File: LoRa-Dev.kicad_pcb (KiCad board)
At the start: 4 copper layers, 72.5 x 71 mm, 19 parts, among them J2 Barrel_Jack_MountingPin, J3 Conn_Coaxial_Small, U1 RPi Pico, U2 LT1963AEQ, U3 RFM95PW

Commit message: E22-900M30S
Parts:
- removed C3: 0.1uF, Capacitor_SMD:C_0603_1608Metric
- removed C4: 47uF, Capacitor_SMD:CP_Elec_6.3x5.8
- removed J3: Conn_Coaxial_Small, Connector_Coaxial:U.FL_Hirose_U.FL-R-SMT-1_Vertical
- removed U3: RFM95PW, LoRa-Dev:RFM95PW
- added C5: 0.1uF, Capacitor_SMD:C_0603_1608Metric, F.Cu at (124.7, 65.5)
- added C6: 47uF, Capacitor_SMD:CP_Elec_6.3x5.8, F.Cu at (125.8, 59.0)
- added J1: Conn_Coaxial_Small, Connector_Coaxial:U.FL_Hirose_U.FL-R-SMT-1_Vertical, F.Cu at (105.2, 53.5)
- added U4: E22-900M30S-SX1262, LoRa-Dev:E22-900M30S-SX1262, F.Cu at (106.8, 79.2)
- moved R9 1.50 mm to (93.5, 48.1)
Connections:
- U1 pad 26: /DIO0 -> /DIO2
- U1 pad 31: unconnected-(U1-GP26-Pad31) -> /BUSY
- U1 pad 32: unconnected-(U1-GP27-Pad32) -> /RXEN
- U1 pad 34: unconnected-(U1-GP28-Pad34) -> /TXEN
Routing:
- net /TXEN: track 0.00 -> 97.2 mm, vias 0 -> 1
- net /RXEN: track 0.00 -> 87.5 mm, vias 0 -> 1
- net /DIO2: track 0.00 -> 55.9 mm, vias 0 -> 2
- net /DIO0: track 52.3 -> 0.00 mm, vias 4 -> 0
- net /BUSY: track 0.00 -> 48.9 mm, vias 0 -> 1
- net GND: track 20.8 -> 52.1 mm, vias 50 -> 54
- net /RESETn: track 25.4 -> 42.8 mm, vias 0 -> 2
- net /SPI_CSn: track 47.3 -> 31.3 mm, vias 3 -> 1
- net /ANT: track 11.1 -> 19.7 mm
- net /DIO1: track 54.5 -> 50.8 mm, vias 4 -> 1
- net /SPI_MISO: track 43.1 -> 39.9 mm
- net /SPI_SCK: track 36.2 -> 33.0 mm
- net RF_VDD: track 109.1 -> 111.7 mm
- net /SPI_MOSI: track 36.4 -> 35.4 mm
- net /RF_GND: vias 29 -> 28

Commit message: updated after first review
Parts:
- removed C6: 47uF, Capacitor_SMD:CP_Elec_6.3x5.8
- added C3: 47uf, Capacitor_SMD:C_1210_3225Metric, F.Cu at (126.8, 59.2)
- moved C5 2.02 mm to (126.7, 65.8)
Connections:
- U4 pad 1: GND -> /RF_GND
- U4 pad 2: GND -> /RF_GND
- U4 pad 20: GND -> /RF_GND
- U4 pad 22: GND -> /RF_GND
- U4 pad 3: GND -> /RF_GND
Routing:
- net GND: track 52.1 -> 20.8 mm, vias 54 -> 46
- net RF_VDD: track 111.7 -> 117.2 mm, vias 6 -> 5
- net /RF_GND: track 0.00 -> 0.90 mm
- net /TXEN: track 97.2 -> 96.4 mm

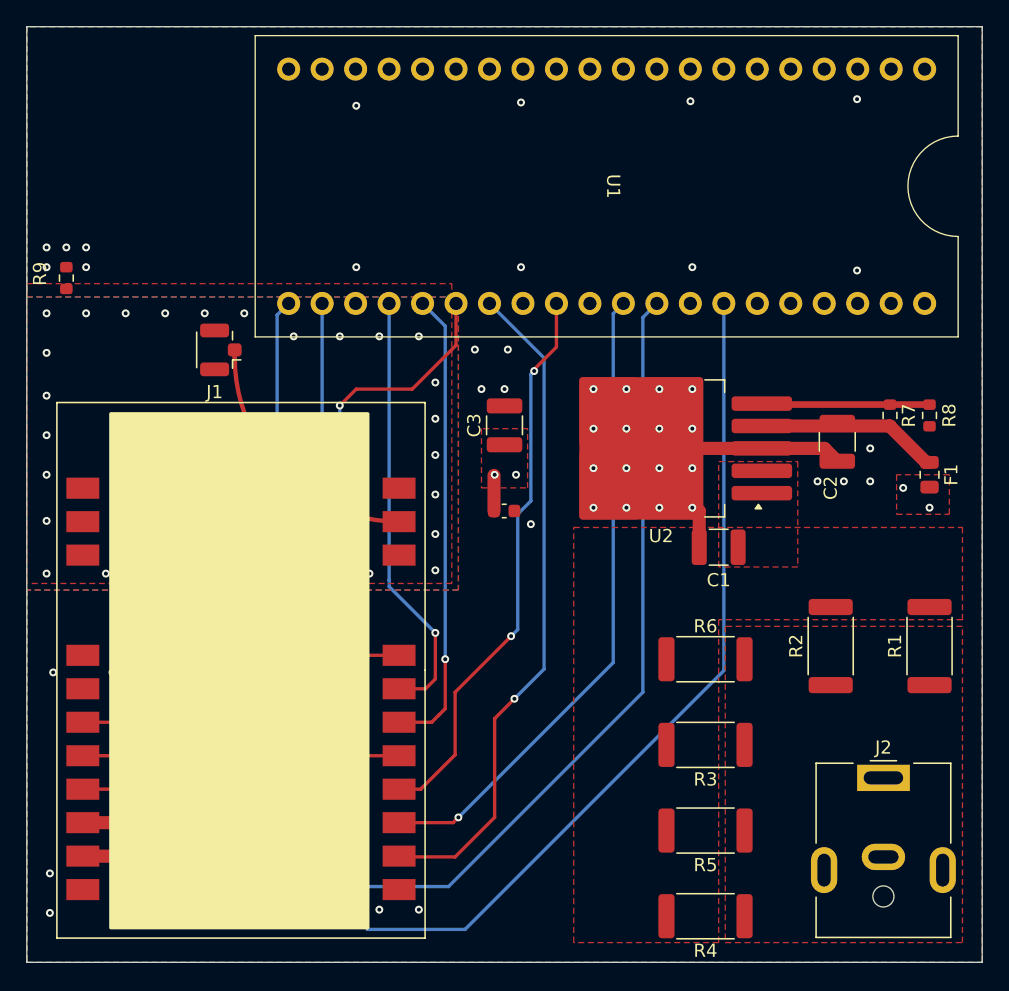
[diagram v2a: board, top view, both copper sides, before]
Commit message: Some fixes, exported BOM
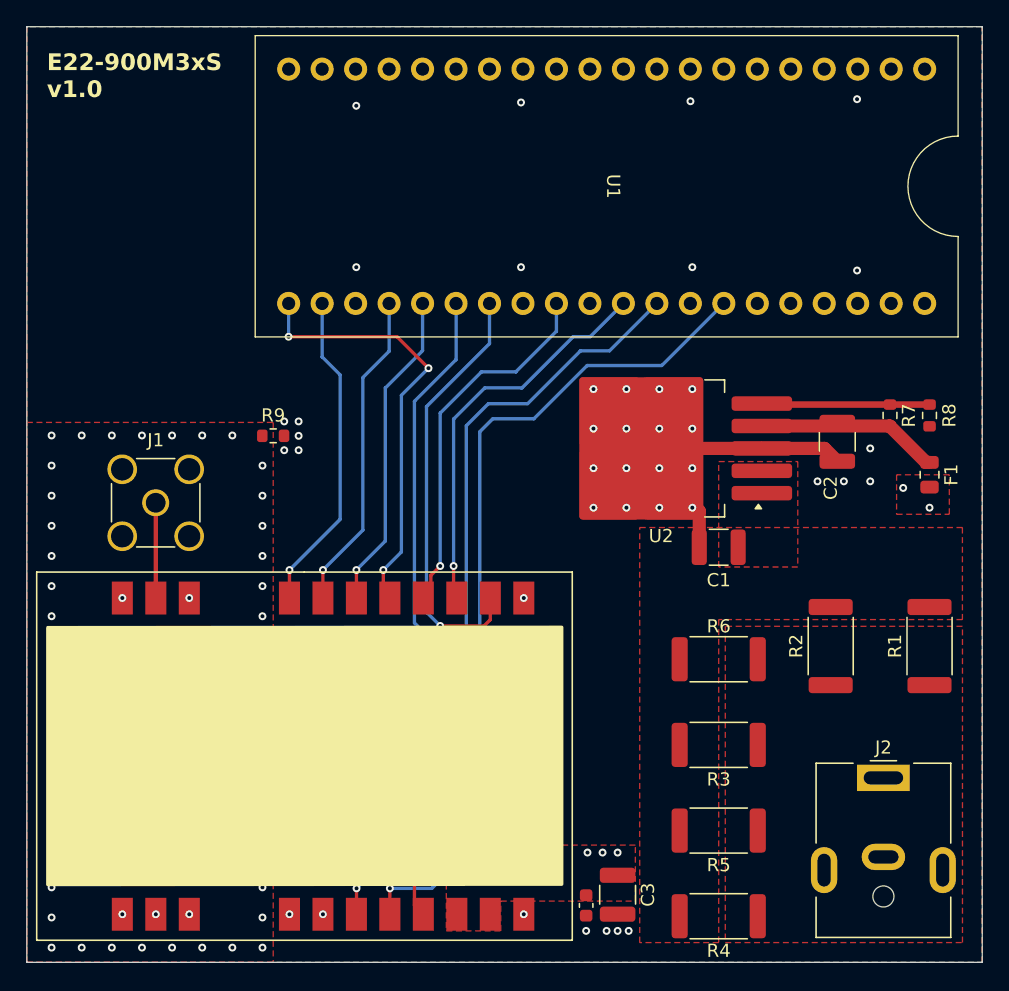
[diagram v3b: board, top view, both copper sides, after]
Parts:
- C3: value 47uf -> 47uF
- J1: value Conn_Coaxial_Small -> SMA; footprint Connector_Coaxial:U.FL_Hirose_U.FL-R-SMT-1_Vertical -> Connector_Coaxial:SMA_Amphenol_901-144_Vertical
- R8: value 1K5 -> 1k5
- moved C3 36.6 mm to (135.3, 94.9), turned to -90 degrees
- moved C5 30.6 mm to (132.9, 95.7), turned to -90 degrees
- moved R9 19.7 mm to (109.2, 60.0), turned to 0 degrees
- moved J1 12.6 mm to (100.3, 65.1), turned to 0 degrees
- moved U4 8.05 mm to (113.0, 84.4), turned to -90 degrees
- moved R3 1.00 mm to (143.0, 83.5)
- moved R4 1.00 mm to (143.0, 96.5)
- moved R5 1.00 mm to (143.0, 90.0)
- moved R6 1.00 mm to (143.0, 77.0)
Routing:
- net RF_VDD: track 117.2 -> 50.2 mm
- net /TXEN: track 96.4 -> 63.9 mm
- net /RXEN: track 87.5 -> 61.2 mm
- net /BUSY: track 48.9 -> 30.2 mm
- net /DIO1: track 50.8 -> 32.5 mm
- net /RESETn: track 42.8 -> 28.1 mm, vias 2 -> 1
- net /ANT: track 19.7 -> 7.23 mm
- net /SPI_MOSI: track 35.4 -> 24.4 mm
- net /SPI_SCK: track 33.0 -> 24.4 mm
- net /SPI_CSn: track 31.3 -> 24.5 mm
- net /SPI_MISO: track 39.9 -> 33.2 mm, vias 1 -> 3
- net /DIO2: track 55.9 -> 50.3 mm, vias 2 -> 1
- net /RF_GND: track 0.90 -> 0.00 mm, vias 28 -> 52
- net GND: vias 46 -> 41
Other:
- board text added: "E22-900M3xS v1.0"
